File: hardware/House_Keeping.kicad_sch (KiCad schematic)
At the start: 4 parts, among them Q13 SI2302DDS-T1-GE3, U15 CD4051BPWR, U16 CD4051BPWR

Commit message: commit
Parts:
- R1: footprint (none) -> footprints:CRCW0603100KFKEAHP; symbol Device:R_US -> CRCW0603100KFKEAHP:CRCW0603100KFKEAHP; Arrow Part Number (none) -> CRCW0603100KFKEAHP; Arrow Price/Stock (none) -> https://www.arrow.com/en/products/crcw0603100kfkeahp/vishay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; Height (none) -> 0.55; Manufacturer_Name (none) -> Vishay; Manufacturer_Part_Number (none) -> CRCW0603100KFKEAHP; Mouser Part Number (none) -> 71-CRCW0603100KFKEAH; Mouser Price/Stock (none) -> https://www.mouser.co.uk/ProductDetail/Vishay-Dale/CRCW0603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
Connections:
- net +3V3: now also R1.2; no longer R1.1
- net at Q13.3 (D), U15.6 (~{E}): now also R1.1; no longer R1.2
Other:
- moved on the sheet: R1
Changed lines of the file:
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@@
     (stroke (width 1) (type default))
   )
-  (wire (pts (xy 109.22 95.25) (xy 116.84 95.25))
+  (wire (pts (xy 107.95 95.25) (xy 116.84 95.25))
     (stroke (width 0) (type default))
   )
@@
     (stroke (width 0) (type default))
   )
-  (wire (pts (xy 93.98 95.25) (xy 101.6 95.25))
-    (stroke (width 0) (type default))
-  )
   (wire (pts (xy 128.27 68.58) (xy 71.12 68.58))
     (stroke (width 0) (type default))
@@
   )
   (wire (pts (xy 63.5 165.1) (xy 45.72 147.32))
+    (stroke (width 0) (type default))
+  )
+  (wire (pts (xy 93.98 95.25) (xy 100.33 95.25))
     (stroke (width 0) (type default))
   )
@@
     )
   )
-  (symbol (lib_id "Device:R_US") (at 105.41 95.25 90) (unit 1)
+  (symbol (lib_id "CRCW0603100KFKEAHP:CRCW0603100KFKEAHP") (at 110.49 95.25 180) (unit 1)
     (in_bom yes) (on_board yes) (dnp no)
-    (property "Reference" "R1" (at 105.3592 93.1672 90)
+    (property "Reference" "R1" (at 105.41 100.33 0)
       (effects (font (size 1.27 1.27)))
     )
-    (property "Value" "100K" (at 105.41 97.79 90)
+    (property "Value" "100K" (at 105.41 97.79 0)
       (effects (font (size 1.27 1.27)))
     )
-    (property "Footprint" "" (at 105.664 94.234 90)
-      (effects (font (size 1.27 1.27)) hide)
-    )
-    (property "Datasheet" "~" (at 105.41 95.25 0)
-      (effects (font (size 1.27 1.27)) hide)
+    (property "Footprint" "footprints:CRCW0603100KFKEAHP" (at 96.52 96.52 0)
+      (effects (font (size 1.27 1.27)) (justify left) hide)
+    )
+    (property "Datasheet" "http://uk.rs-online.com/web/p/products/1823583" (at 96.52 93.98 0)
+      (effects (font (size 1.27 1.27)) (justify left) hide)
+    )
+    (property "Description" "VISHAY - CRCW0603100KFKEAHP - SMD Chip Resistor, 0603 [1608 Metric], 100 kohm, CRCW-HP e3 Series, 75 V, Thick Film, 250 mW" (at 96.52 91.44 0)
+      (effects (font (size 1.27 1.27)) (justify left) hide)
+    )
+    (property "Height" "0.55" (at 96.52 88.9 0)
+      (effects (font (size 1.27 1.27)) (justify left) hide)
+    )
+    (property "Manufacturer_Name" "Vishay" (at 96.52 86.36 0)
+      (effects (font (size 1.27 1.27)) (justify left) hide)
+    )
+    (property "Manufacturer_Part_Number" "CRCW0603100KFKEAHP" (at 96.52 83.82 0)
+      (effects (font (size 1.27 1.27)) (justify left) hide)
+    )
+    (property "Mouser Part Number" "71-CRCW0603100KFKEAH" (at 96.52 81.28 0)
+      (effects (font (size 1.27 1.27)) (justify left) hide)
+    )
+    (property "Mouser Price/Stock" "https://www.mouser.co.uk/ProductDetail/Vishay-Dale/CRCW0603100KFKEAHP?qs=niDbCuOAQ0Uxys8g4tQWNQ%3D%3D" (at 96.52 78.74 0)
+      (effects (font (size 1.27 1.27)) (justify left) hide)
+    )
+    (property "Arrow Part Number" "CRCW0603100KFKEAHP" (at 96.52 76.2 0)
+      (effects (font (size 1.27 1.27)) (justify left) hide)
+    )
+    (property "Arrow Price/Stock" "https://www.arrow.com/en/products/crcw0603100kfkeahp/vishay?region=nac" (at 96.52 73.66 0)
+      (effects (font (size 1.27 1.27)) (justify left) hide)
     )
     (pin "1")

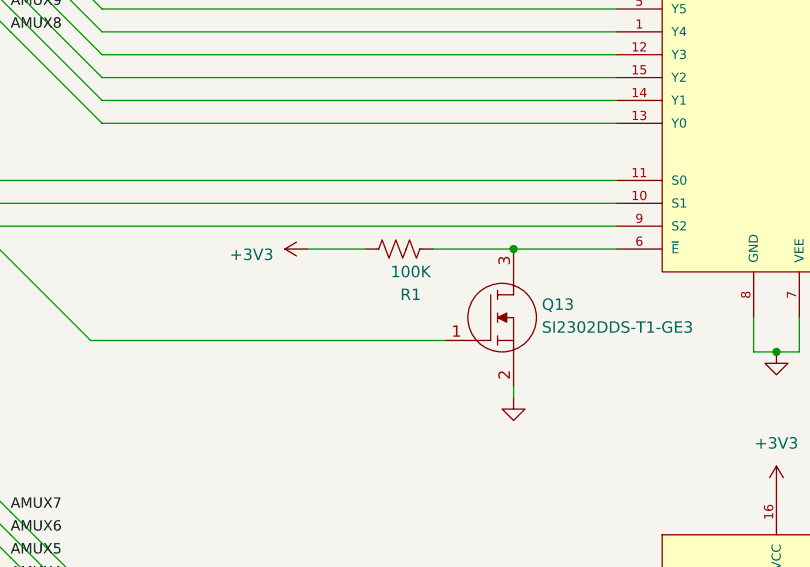
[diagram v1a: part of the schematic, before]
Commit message: hardware: All resistors added.
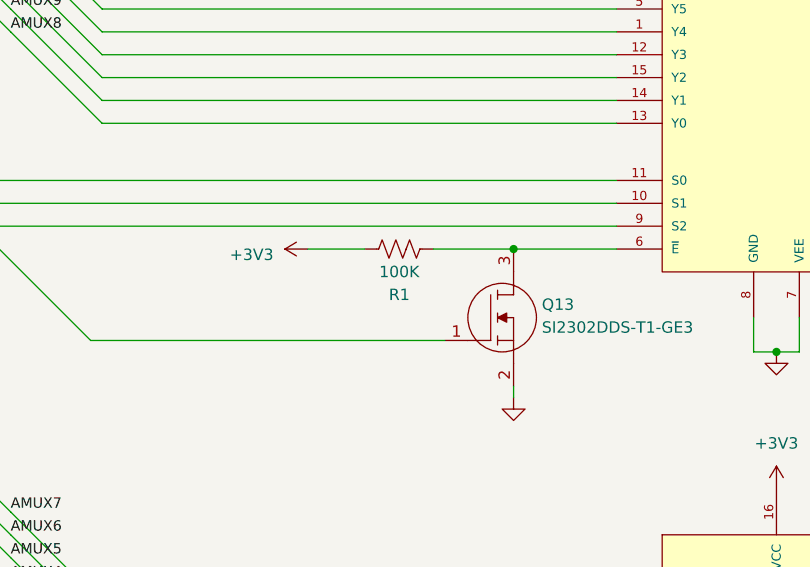
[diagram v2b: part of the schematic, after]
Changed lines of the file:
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@@
   (symbol (lib_id "CRCW0603100KFKEAHP:CRCW0603100KFKEAHP") (at 110.49 95.25 180) (unit 1)
     (in_bom yes) (on_board yes) (dnp no)
-    (property "Reference" "R1" (at 105.41 100.33 0)
+    (property "Reference" "R1" (at 104.14 100.33 0)
       (effects (font (size 1.27 1.27)))
     )
-    (property "Value" "100K" (at 105.41 97.79 0)
+    (property "Value" "100K" (at 104.14 97.79 0)
       (effects (font (size 1.27 1.27)))
     )

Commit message: hardware: starting the pcb project
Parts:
- removed Q13: SI2302DDS-T1-GE3, footprints:SI2302DDS-T1-GE3, symbol SI2302DDS-T1-GE3:SI2302DDS-T1-GE3
- added Q7: SI2302DDS-T1-GE3, footprints:SI2302DDS-T1-GE3, symbol SI2302DDS-T1-GE3:SI2302DDS-T1-GE3
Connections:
- net AMUX_SEL3: now also Q7.1 (G)
- net GND: now also Q7.2 (S)
- net at R1.1, U15.6 (~{E}): now also Q7.3 (D)
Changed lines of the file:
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@@
 (kicad_sch (version 20230121) (generator eeschema)
   (paper "A4")
+  (junction (at 116.84 95.25) (diameter 0) (color 0 0 0 0)
+  )
   (junction (at 173.99 110.49) (diameter 0) (color 0 0 0 0)
   )
@@
   (junction (at 146.05 182.88) (diameter 0) (color 0 0 0 0)
   )
-  (junction (at 116.84 95.25) (diameter 0) (color 0 0 0 0)
-  )
   (bus_entry (at 43.18 76.2) (size 2.54 2.54)
     (stroke (width 0) (type default))
@@
     (stroke (width 0) (type default))
   )
+  (wire (pts (xy 116.84 95.25) (xy 128.27 95.25))
+    (stroke (width 0) (type default))
+  )
   (bus (pts (xy 58.42 137.16) (xy 58.42 139.7))
     (stroke (width 1) (type default))
@@
   )
   (wire (pts (xy 63.5 170.18) (xy 45.72 152.4))
-    (stroke (width 0) (type default))
-  )
-  (wire (pts (xy 116.84 95.25) (xy 128.27 95.25))
     (stroke (width 0) (type default))
   )
@@
         (path "/2eebaa11-d7ed-4bfd-bc8e-988f68654d29/091c188d-8c4a-409e-952c-8d45a0b217b0"
           (reference "#PWR063") (unit 1)
+        )
+      )
+    )
+  )
+  (symbol (lib_id "SI2302DDS-T1-GE3:SI2302DDS-T1-GE3") (at 109.22 105.41 0) (unit 1)
+    (in_bom yes) (on_board yes) (dnp no) (fields_autoplaced)
+    (property "Reference" "Q7" (at 120.65 102.235 0)
+      (effects (font (size 1.27 1.27)) (justify left))
+    )
+    (property "Value" "SI2302DDS-T1-GE3" (at 120.65 104.775 0)
+      (effects (font (size 1.27 1.27)) (justify left))
+    )
+    (property "Footprint" "footprints:SI2302DDS-T1-GE3" (at 97.79 139.7 0)
+      (effects (font (size 1.27 1.27)) (justify left top) hide)
+    )
+    (property "Datasheet" "http://www.vishay.com/docs/63653/si2302dds.pdf" (at 84.836 142.494 0)
+      (effects (font (size 1.27 1.27)) (justify left top) hide)
+    )
+    (property "Height" "1.12" (at 120.65 504.14 0)
+      (effects (font (size 1.27 1.27)) (justify left top) hide)
+    )
+    (property "Mouser Part Number" "78-SI2302DDS-T1-GE3" (at 120.65 604.14 0)
+      (effects (font (size 1.27 1.27)) (justify left top) hide)
+    )
+    (property "Mouser Price/Stock" "https://www.mouser.co.uk/ProductDetail/Vishay-Semiconductors/SI2302DDS-T1-GE3?qs=MxnWX8BLHKdaCSNWhg%252BxLA%3D%3D" (at 120.65 704.14 0)
+      (effects (font (size 1.27 1.27)) (justify left top) hide)
+    )
+    (property "Manufacturer_Name" "Vishay" (at 120.65 804.14 0)
+      (effects (font (size 1.27 1.27)) (justify left top) hide)
+    )
+    (property "Manufacturer_Part_Number" "SI2302DDS-T1-GE3" (at 120.65 904.14 0)
+      (effects (font (size 1.27 1.27)) (justify left top) hide)
+    )
+    (pin "1")
+    (pin "2")
+    (pin "3")
+    (instances
+      (project "eps-re_project"
+        (path "/2eebaa11-d7ed-4bfd-bc8e-988f68654d29/091c188d-8c4a-409e-952c-8d45a0b217b0"
+          (reference "Q7") (unit 1)
         )
       )
@@
         )
       )
-    )
-  )
-  (symbol (lib_id "SI2302DDS-T1-GE3:SI2302DDS-T1-GE3") (at 109.22 105.41 0) (unit 1)
-    (in_bom yes) (on_board yes) (dnp no)
-    (property "Reference" "Q13" (at 119.9775 101.4231 0)
-      (effects (font (size 1.27 1.27)) (justify left))
-    )
-    (property "Value" "SI2302DDS-T1-GE3" (at 119.9775 103.9631 0)
-      (effects (font (size 1.27 1.27)) (justify left))
-    )
-    (property "Footprint" "footprints:SI2302DDS-T1-GE3" (at 97.79 139.7 0) (show_name)
-      (effects (font (size 1.27 1.27)) (justify left top) hide)
-    )
-    (property "Datasheet" "http://www.vishay.com/docs/63653/si2302dds.pdf" (at 84.836 142.494 0) (show_name)
-      (effects (font (size 1.27 1.27)) (justify left top) hide)
-    )
-    (property "Height" "1.12" (at 120.65 504.14 0)
-      (effects (font (size 1.27 1.27)) (justify left top) hide)
-    )
-    (property "Mouser Part Number" "78-SI2302DDS-T1-GE3" (at 120.65 604.14 0)
-      (effects (font (size 1.27 1.27)) (justify left top) hide)
-    )
-    (property "Mouser Price/Stock" "https://www.mouser.co.uk/ProductDetail/Vishay-Semiconductors/SI2302DDS-T1-GE3?qs=MxnWX8BLHKdaCSNWhg%252BxLA%3D%3D" (at 120.65 704.14 0)
-      (effects (font (size 1.27 1.27)) (justify left top) hide)
-    )
-    (property "Manufacturer_Name" "Vishay" (at 120.65 804.14 0)
-      (effects (font (size 1.27 1.27)) (justify left top) hide)
-    )
-    (property "Manufacturer_Part_Number" "SI2302DDS-T1-GE3" (at 120.65 904.14 0)
-      (effects (font (size 1.27 1.27)) (justify left top) hide)
-    )
-    (pin "1")
-    (pin "2")
-    (pin "3")
-    (instances
-      (project "eps-re_project"
-        (path "/2eebaa11-d7ed-4bfd-bc8e-988f68654d29/091c188d-8c4a-409e-952c-8d45a0b217b0"
-          (reference "Q13") (unit 1)
-        )
-      )

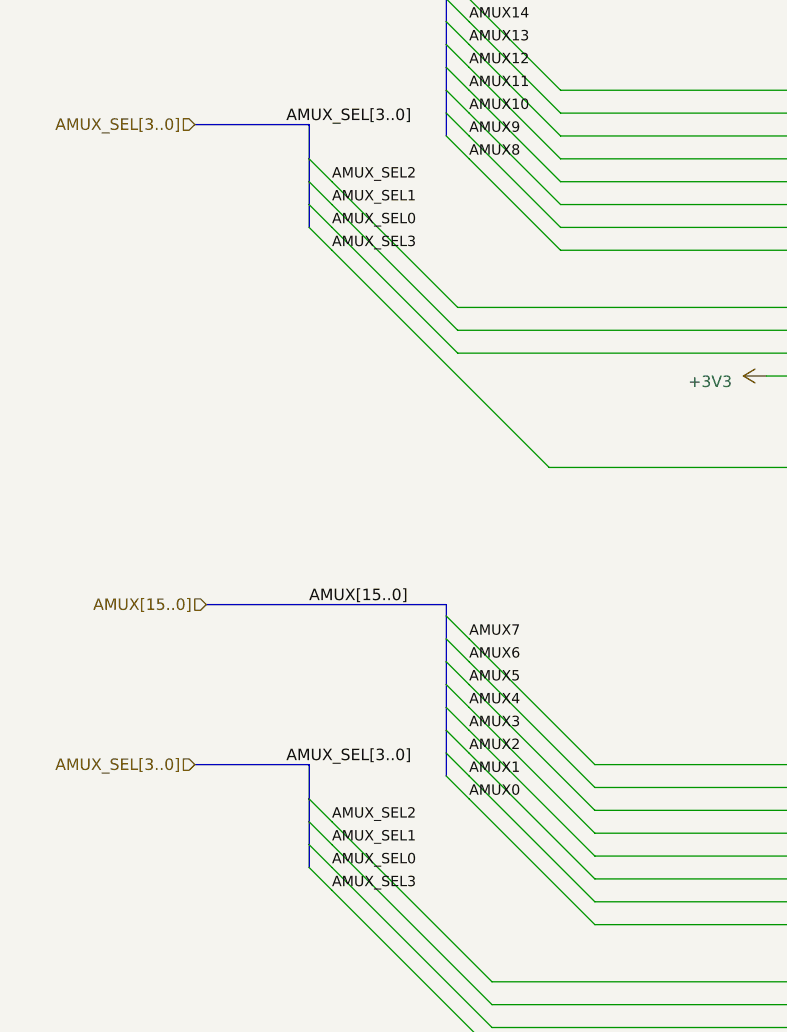
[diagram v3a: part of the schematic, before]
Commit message: hardware: Updating the schematic considering issues #2, #3, #4, #5 and #6.
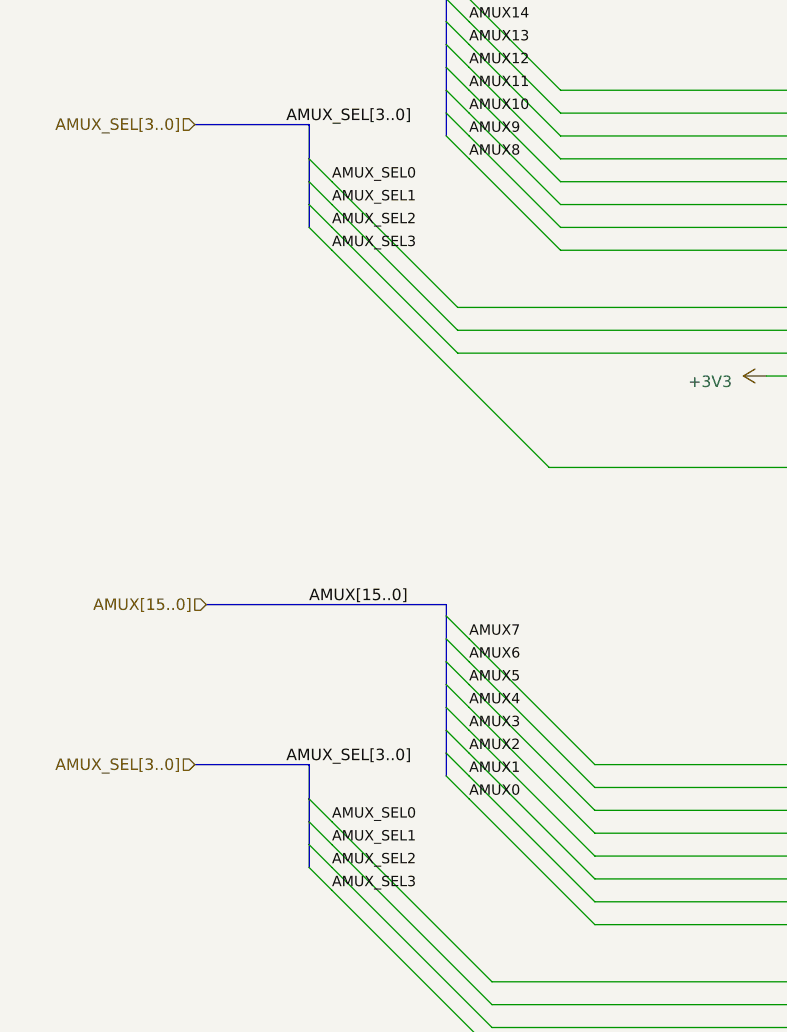
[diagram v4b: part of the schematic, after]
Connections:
- net AMUX_SEL0: now also U15.11 (S0), U16.11 (S0); no longer U15.9 (S2), U16.9 (S2)
- net AMUX_SEL2: now also U15.9 (S2), U16.9 (S2); no longer U15.11 (S0), U16.11 (S0)
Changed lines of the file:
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@@
     (effects (font (size 1.15 1.15)) (justify left bottom))
   )
-  (label "AMUX_SEL0" (at 45.72 78.74 0) (fields_autoplaced)
+  (label "AMUX_SEL0" (at 45.72 73.66 0) (fields_autoplaced)
     (effects (font (size 1.15 1.15)) (justify left bottom))
   )
@@
     (effects (font (size 1.15 1.15)) (justify left bottom))
   )
-  (label "AMUX_SEL2" (at 45.72 73.66 0) (fields_autoplaced)
+  (label "AMUX_SEL2" (at 45.72 78.74 0) (fields_autoplaced)
     (effects (font (size 1.15 1.15)) (justify left bottom))
   )
@@
     (effects (font (size 1.15 1.15)) (justify left bottom))
   )
-  (label "AMUX_SEL2" (at 45.72 144.78 0) (fields_autoplaced)
+  (label "AMUX_SEL2" (at 45.72 149.86 0) (fields_autoplaced)
     (effects (font (size 1.15 1.15)) (justify left bottom))
   )
@@
     (effects (font (size 1.15 1.15)) (justify left bottom))
   )
-  (label "AMUX_SEL0" (at 45.72 149.86 0) (fields_autoplaced)
+  (label "AMUX_SEL0" (at 45.72 144.78 0) (fields_autoplaced)
     (effects (font (size 1.15 1.15)) (justify left bottom))
   )

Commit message: hardware: Updating 3D models, component placement and more.
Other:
- title: (none) -> Reliability Enhanced Electrical Power System
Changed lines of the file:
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@@
 (kicad_sch (version 20230121) (generator eeschema)
   (paper "A4")
+  (title_block
+    (title "Reliability Enhanced Electrical Power System")
+    (date "2023-08-03")
+    (rev "v0.0")
+    (comment 1 "João C. E. Barcellos <joaoclaudiobarcellos@gmail.com>")
+    (comment 2 "Laura Debastiani <laudebastiani@gmail.com>")
+  )
   (junction (at 116.84 95.25) (diameter 0) (color 0 0 0 0)
   )

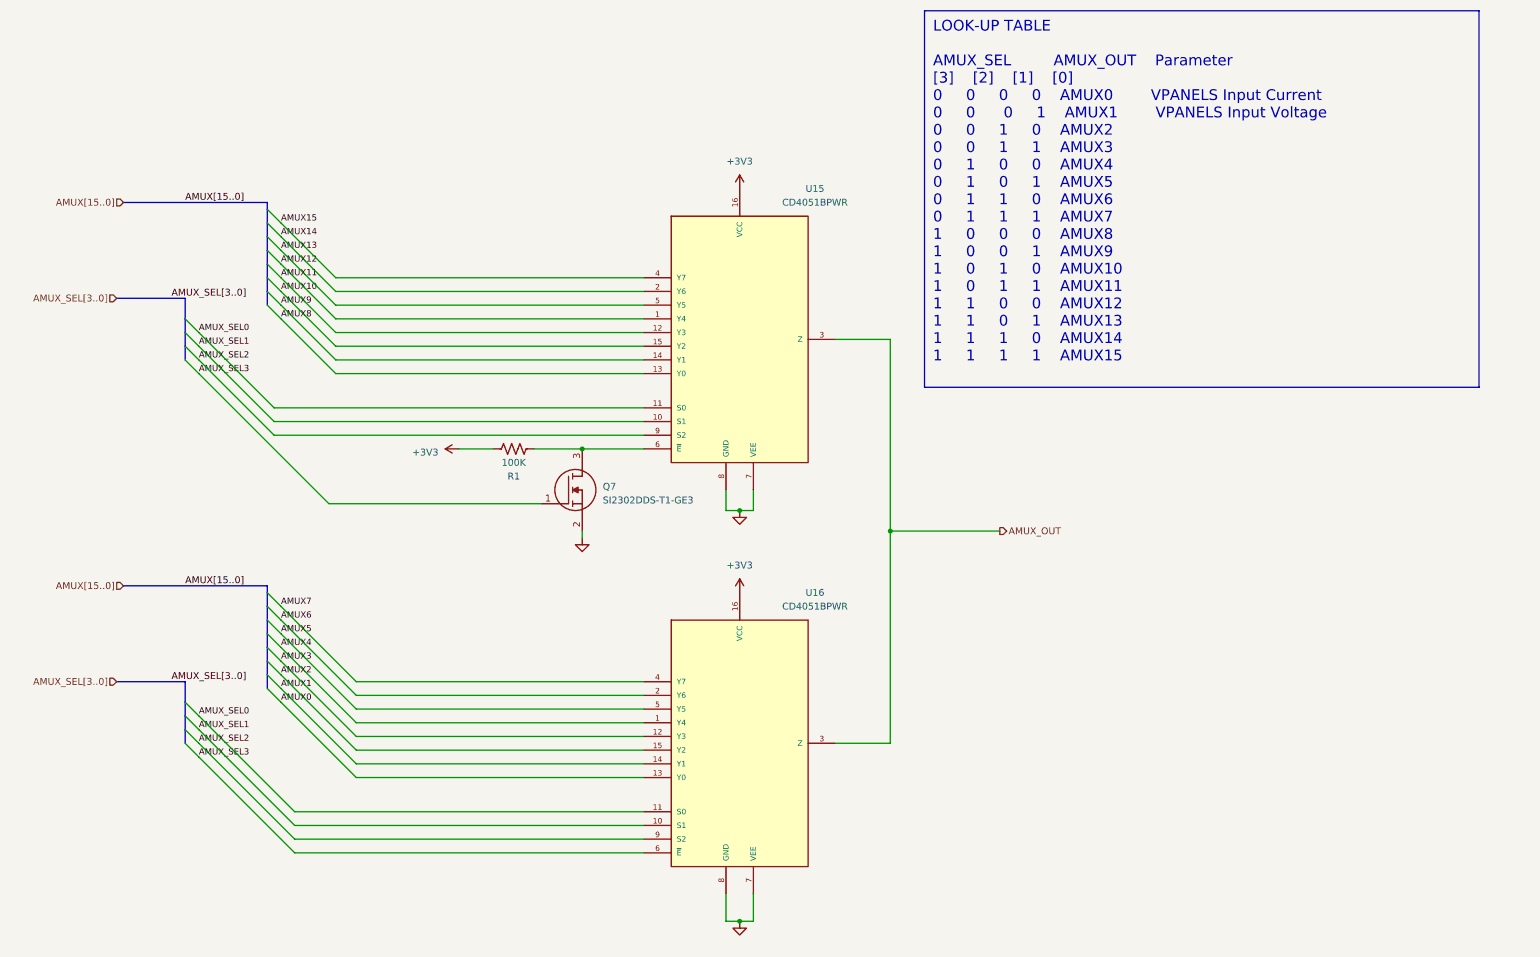
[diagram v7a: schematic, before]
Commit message: hardware: Updating the MPPT circuit.
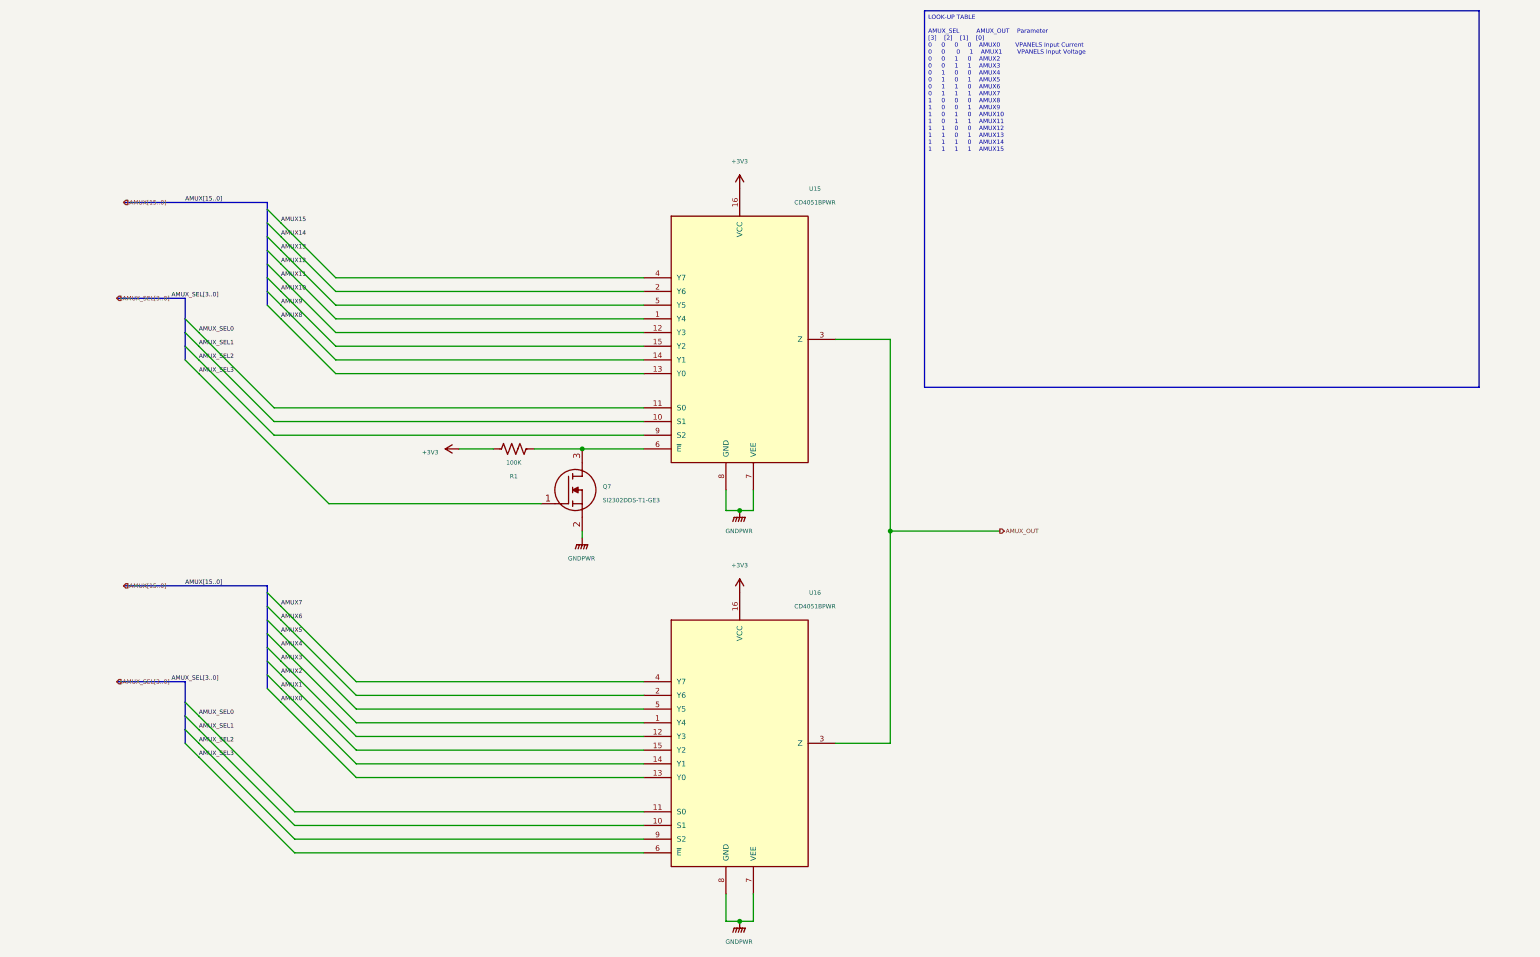
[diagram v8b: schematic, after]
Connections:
- net GND renamed GNDPWR
